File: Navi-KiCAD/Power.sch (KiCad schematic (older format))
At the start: 20 parts, among them Q1 IRLML5203TRPBF, Q2 IRLML5203TRPBF, U10 TPS54232DR, U14 LTC4412ES6#TRPBF, U15 MIC94082YFT-TR

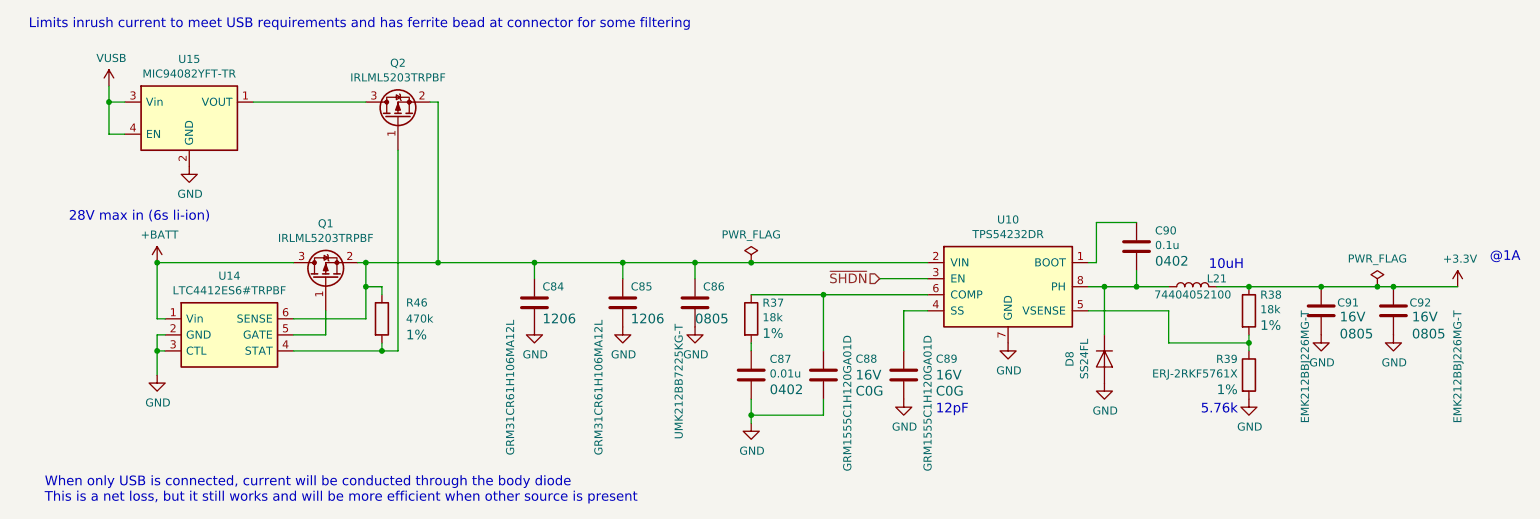
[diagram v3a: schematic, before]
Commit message: Upgraded to 9 channel RGB driver. Broke out signals for LSM303 and LSM6DS3
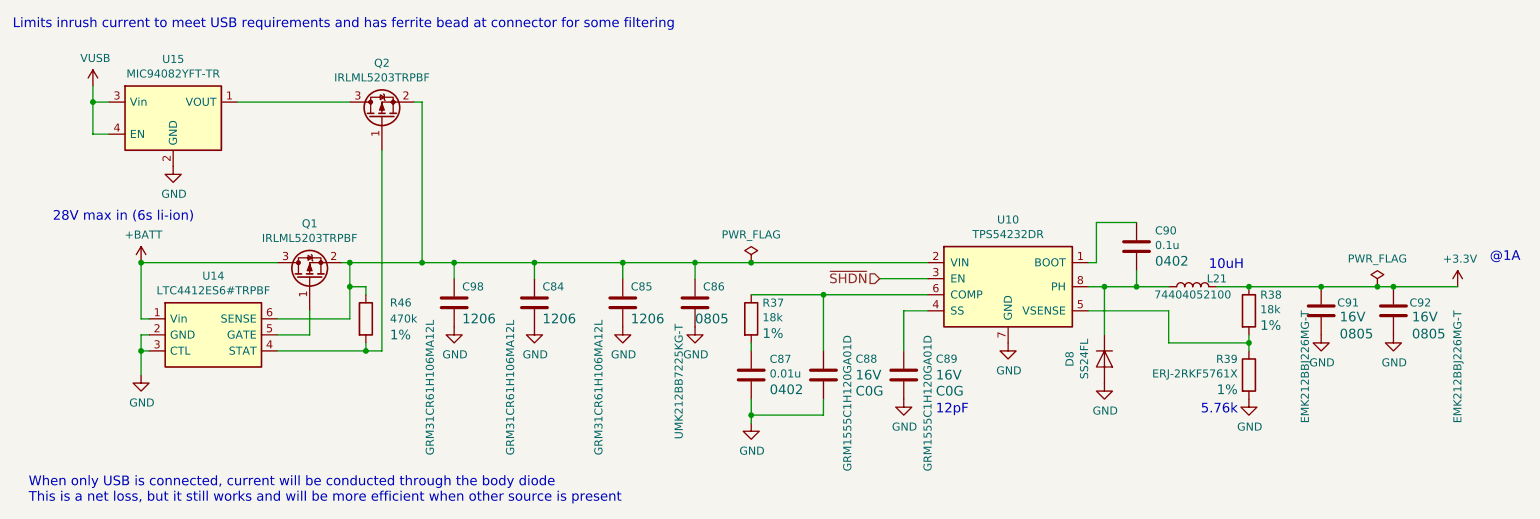
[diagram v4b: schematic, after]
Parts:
- added C98: GRM31CR61H106MA12L, Capacitors_SMD:C_1206, symbol C
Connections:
- net GND: now also C98.2
- net at C84.1, C85.1, C86.1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: now also C98.1
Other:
- moved on the sheet: Q1, Q2, R46, U14, U15
